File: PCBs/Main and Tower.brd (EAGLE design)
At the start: 74 x 83 mm, 22 parts

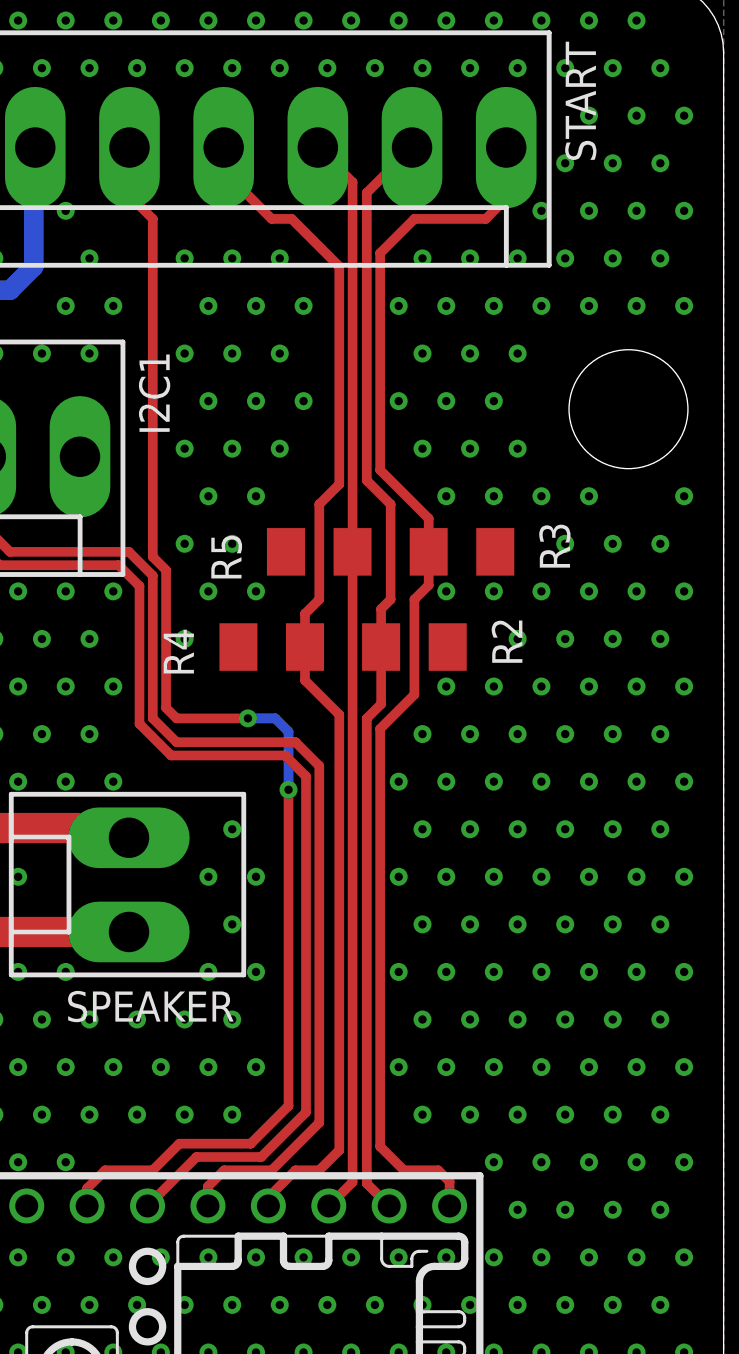
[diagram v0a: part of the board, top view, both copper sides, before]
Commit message: Issues #6 and #9
This Addresses Issues #6 and #9
Code Changes:
1.	Relay Pin order had to be reversed
2.	Record_Lap and lap_time changed from unsigned short to unsigned long
3.	Penalty_LaneX (1-4) changed from 0 to 1 to work with change to PULLUP on Lap Pins
4.	Changed pinmode for LANEXLAP (1-4) from INPUT to INPUT_PULLUP
5.	Moved Last Lap Monitoring from Race Metrics to Main Loop
6.	On Race end the menu will skip Welcome Function (Users didn’t want to wait for the sound/lights to finish)
7.	Changed Lap Record reset value from 10000 to 99999
8.	Changed Penalty_LaneX triggers from 1 to 0 to work with PinMode Change
9.	Changed Lap read from HIGH to LOW to work with PinMode Change
10.	Change track debounce compare to correct factore to function as intended
11.	Added “FL” display on Lap Counter
PCB Changes:
1.	Removed R2-R5 and Replaced them with C2-C5 (0.1uF Capacitors)
2.	Added C1 (16V 4700uF) and R1 (82) Values
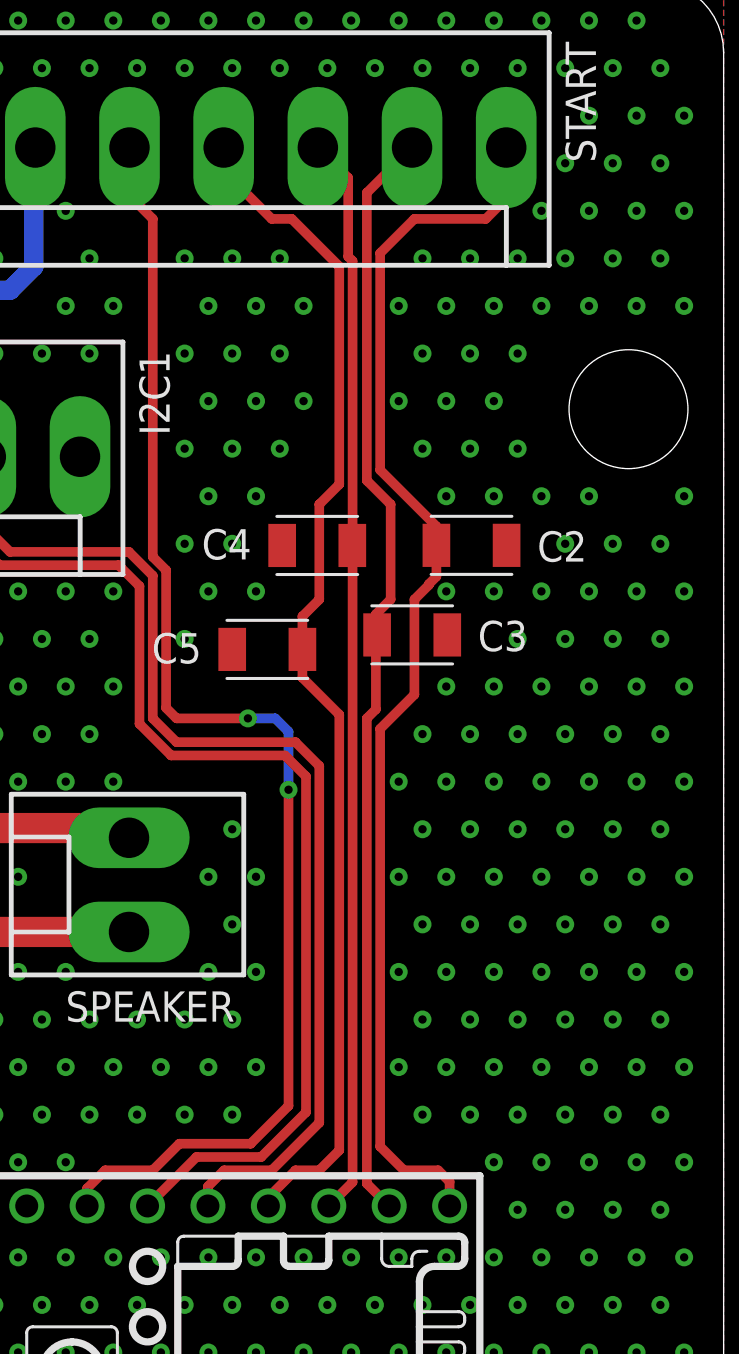
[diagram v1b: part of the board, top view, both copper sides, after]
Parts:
- removed R2, R3, R4, R5: 10k, adafruit:M1206
- added C2, C3, C4, C5: 0.1uF, Capacitor:CAPC3216X135
- C1: value (none) -> 16V 4700uF
- R6: value 100k -> 82
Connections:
- net GND: now also C2.2, C3.2, C4.2, C5.2; no longer R2.1, R3.1, R4.1, R5.1
- net L1LAP: now also C2.1; no longer R3.2
- net L2LAP: now also C3.1; no longer R2.2
- net L3LAP: now also C4.1; no longer R5.2
- net L4LAP: now also C5.1; no longer R4.2
